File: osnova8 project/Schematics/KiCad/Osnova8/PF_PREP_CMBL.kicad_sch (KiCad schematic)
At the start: 10 parts, among them U38 74LS08, U39 74LS08, U41 74LS00, U42 74LS00

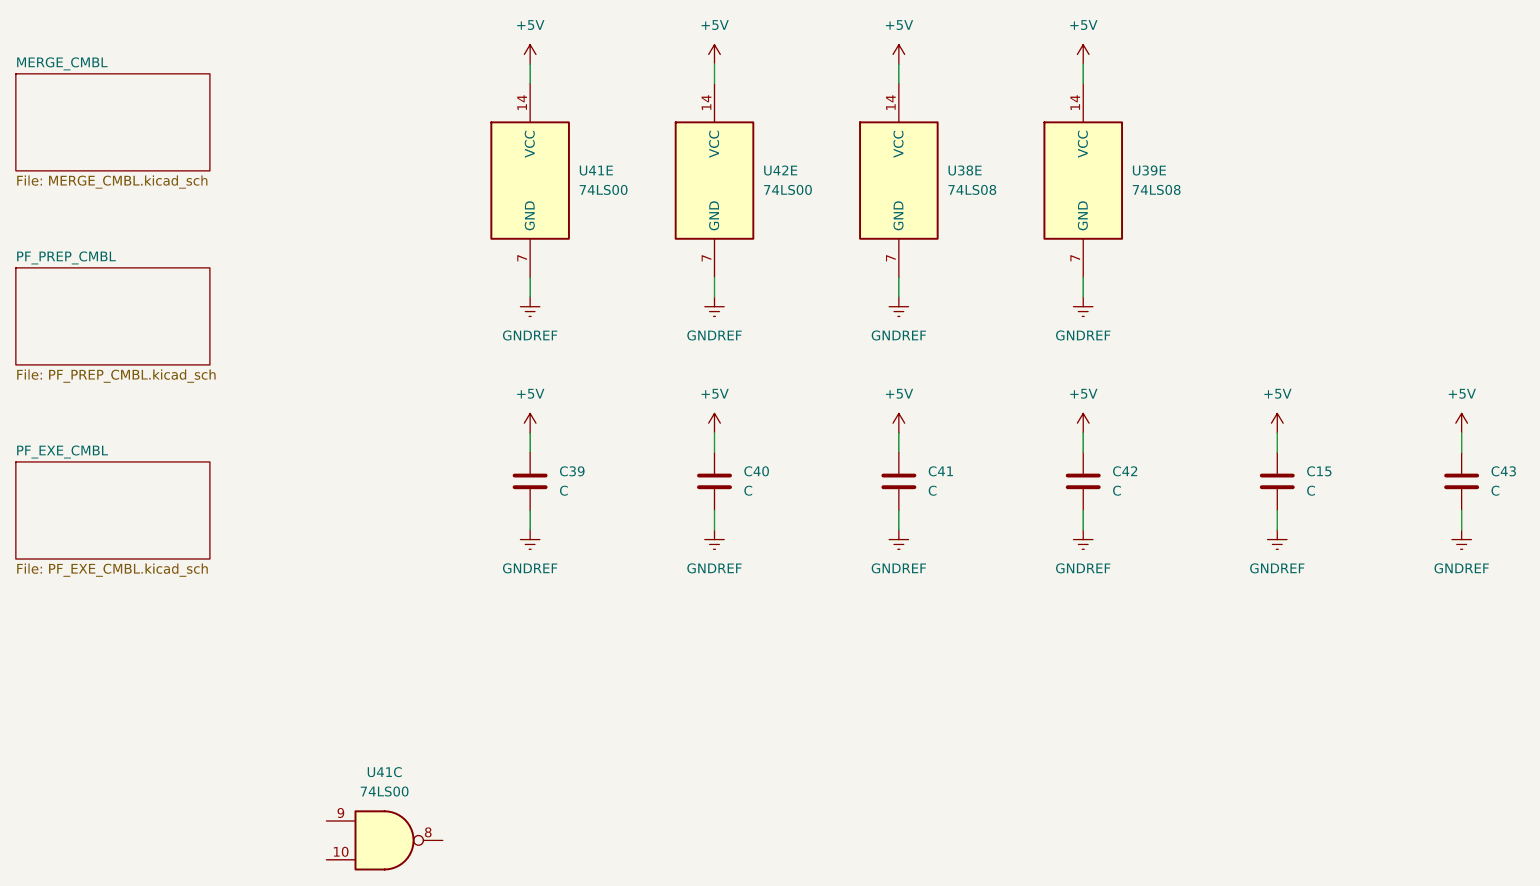
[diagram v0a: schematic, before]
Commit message: updated schematics
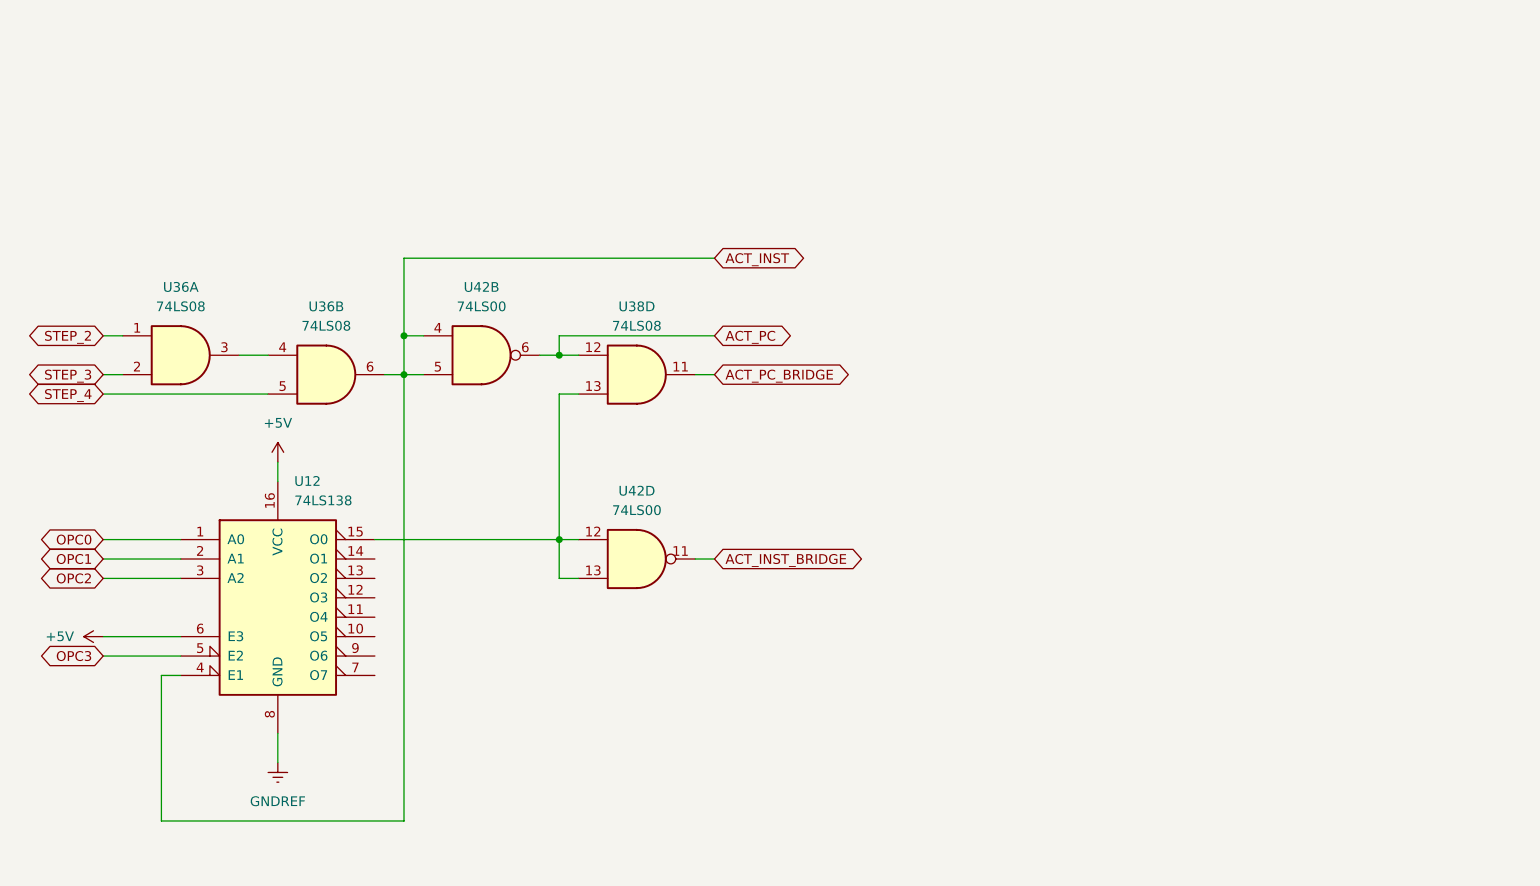
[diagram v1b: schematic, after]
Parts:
- removed C15, C39, C40, C41, C42, C43: C, symbol Device:C
- removed U38, U39: 74LS08, symbol 74xx:74LS08
- removed U41, U42: 74LS00, symbol 74xx:74LS00
- added U12: 74LS138, symbol 74xx:74LS138
- added U36, U38: 74LS08, symbol 74xx:74LS08
- added U42: 74LS00, symbol 74xx:74LS00
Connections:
- net +5V: now also U12.16 (VCC), U12.6 (E3)
- net GNDREF: now also U12.8 (GND)
- new net: U36.3, U36.4
- new net: U12.15 (O0), U38.13, U42.12, U42.13
- new net ACT_INST: U12.4 (E1), U36.6, U42.4, U42.5
- new net ACT_INST_BRIDGE: U42.11
- new net ACT_PC: U38.12, U42.6
- new net ACT_PC_BRIDGE: U38.11
- new net OPC0: U12.1 (A0)
- new net OPC1: U12.2 (A1)
- new net OPC2: U12.3 (A2)
- new net OPC3: U12.5 (E2)
- new net STEP_2: U36.1
- new net STEP_3: U36.2
- new net STEP_4: U36.5
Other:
- removed sheet MERGE_CMBL
- removed sheet PF_EXE_CMBL
- removed sheet PF_PREP_CMBL
